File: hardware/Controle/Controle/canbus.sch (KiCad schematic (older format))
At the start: 5 parts, among them U201 MCP2561-E-SN

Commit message: first version of layout
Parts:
- added C202: 4.7n, Capacitor_SMD:C_0603_1608Metric_Pad1.08x0.95mm_HandSolder, symbol Device:C_Small
- added R203: 300, Resistor_SMD:R_0603_1608Metric_Pad0.98x0.95mm_HandSolder, symbol Device:R_Small
- added R204, R205: 60, Resistor_SMD:R_0603_1608Metric_Pad0.98x0.95mm_HandSolder, symbol Device:R_Small
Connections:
- net CAN_H: now also R204.2
- net CAN_L: now also R205.1
- net GND: now also C202.2
- net at U201.5 (SPLIT): now also R203.2
- new net: C202.1, R203.1, R204.1, R205.2
- no-connect marks 1 -> 0
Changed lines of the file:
@@
 $EndDescr
 Wire Wire Line
-	5750 3350 6450 3350
-Wire Wire Line
-	5750 3550 6450 3550
+	5750 3000 6200 3000
+Wire Wire Line
+	5750 3900 6200 3900
 Connection ~ 5250 4000
 $Comp
@@
 	0    -1   -1   0
 $EndComp
-Text Label 6200 3350 0    50   ~ 0
+Text Label 6500 3000 2    50   ~ 0
 CAN_H
-Text Label 6200 3550 0    50   ~ 0
+Text Label 6550 3900 2    50   ~ 0
 CAN_L
-Text HLabel 6450 3350 2    50   Input ~ 0
+Text HLabel 6500 3000 2    50   Input ~ 0
 CAN_H
-Text HLabel 6450 3550 2    50   Input ~ 0
+Text HLabel 6550 3900 2    50   Input ~ 0
 CAN_L
 Text HLabel 4200 3250 0    50   Input ~ 0
@@
 	1    0    0    -1
 $EndComp
-NoConn ~ 5750 3450
 Wire Wire Line
 	7050 4600 7050 4500
+Wire Wire Line
+	5750 3000 5750 3350
+Wire Wire Line
+	5750 3900 5750 3550
+$Comp
+L Device:R_Small R?
+U 1 1 60A1B053
+P 6000 3450
+AR Path="/60A1B053" Ref="R?"  Part="1"
+AR Path="/606C6891/60A1B053" Ref="R203"  Part="1"
+F 0 "R203" H 6059 3496 50  0000 L CNN
+F 1 "300" H 6059 3405 50  0000 L CNN
+F 2 "Resistor_SMD:R_0603_1608Metric_Pad0.98x0.95mm_HandSolder" H 6000 3450 50  0001 C CNN
+F 3 "~" H 6000 3450 50  0001 C CNN
+	1    6000 3450
+	0    1    1    0
+$EndComp
+Wire Wire Line
+	5900 3450 5750 3450
+$Comp
+L Device:R_Small R?
+U 1 1 60A1D2BE
+P 6200 3250
+AR Path="/60A1D2BE" Ref="R?"  Part="1"
+AR Path="/606C6891/60A1D2BE" Ref="R204"  Part="1"
+F 0 "R204" H 6259 3296 50  0000 L CNN
+F 1 "60" H 6259 3205 50  0000 L CNN
+F 2 "Resistor_SMD:R_0603_1608Metric_Pad0.98x0.95mm_HandSolder" H 6200 3250 50  0001 C CNN
+F 3 "~" H 6200 3250 50  0001 C CNN
+	1    6200 3250
+	1    0    0    1
+$EndComp
+Wire Wire Line
+	6200 3550 6200 3450
+Wire Wire Line
+	6100 3450 6200 3450
+Connection ~ 6200 3450
+Wire Wire Line
+	6200 3450 6200 3350
+Wire Wire Line
+	6200 3750 6200 3900
+Connection ~ 6200 3900
+Wire Wire Line
+	6200 3900 6550 3900
+$Comp
+L Device:R_Small R?
+U 1 1 60A1D7FB
+P 6200 3650
+AR Path="/60A1D7FB" Ref="R?"  Part="1"
+AR Path="/606C6891/60A1D7FB" Ref="R205"  Part="1"
+F 0 "R205" H 6259 3696 50  0000 L CNN
+F 1 "60" H 6259 3605 50  0000 L CNN
+F 2 "Resistor_SMD:R_0603_1608Metric_Pad0.98x0.95mm_HandSolder" H 6200 3650 50  0001 C CNN
+F 3 "~" H 6200 3650 50  0001 C CNN
+	1    6200 3650
+	1    0    0    1
+$EndComp
+Wire Wire Line
+	6200 3150 6200 3000
+Connection ~ 6200 3000
+Wire Wire Line
+	6200 3000 6500 3000
+$Comp
+L Device:C_Small C?
+U 1 1 60A214AF
+P 6600 3450
+AR Path="/60A214AF" Ref="C?"  Part="1"
+AR Path="/606C6891/60A214AF" Ref="C202"  Part="1"
+F 0 "C202" V 6829 3450 50  0000 C CNN
+F 1 "4.7n" V 6738 3450 50  0000 C CNN
+F 2 "Capacitor_SMD:C_0603_1608Metric_Pad1.08x0.95mm_HandSolder" H 6600 3450 50  0001 C CNN
+F 3 "~" H 6600 3450 50  0001 C CNN
+	1    6600 3450
+	0    -1   -1   0
+$EndComp
+Wire Wire Line
+	6500 3450 6200 3450
+$Comp
+L power:GND #PWR?
+U 1 1 60A223CF
+P 6900 3500
+AR Path="/60A223CF" Ref="#PWR?"  Part="1"
+AR Path="/606C6891/60A223CF" Ref="#PWR0129"  Part="1"
+F 0 "#PWR0129" H 6900 3250 50  0001 C CNN
+F 1 "GND" H 6905 3327 50  0000 C CNN
+F 2 "" H 6900 3500 50  0001 C CNN
+F 3 "" H 6900 3500 50  0001 C CNN
+	1    6900 3500
+	1    0    0    -1
+$EndComp
+Wire Wire Line
+	6900 3500 6900 3450
+Wire Wire Line
+	6900 3450 6700 3450
 $EndSCHEMATC

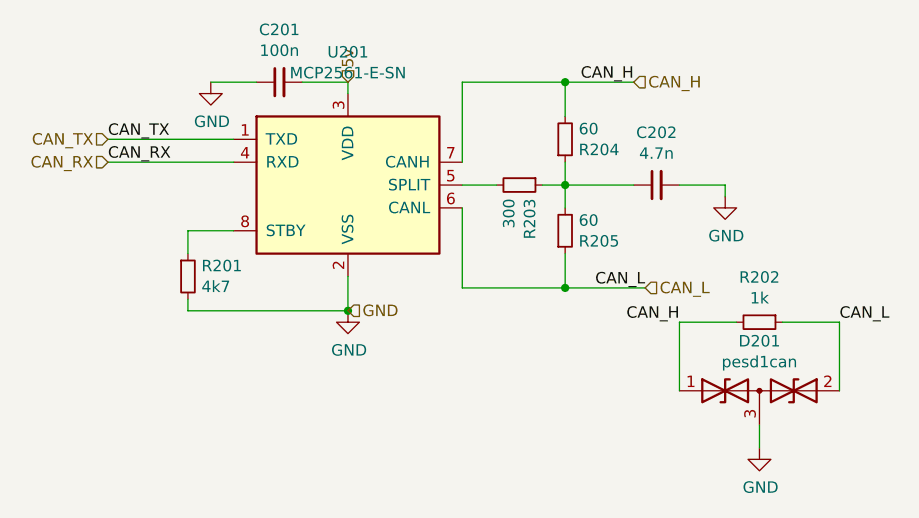
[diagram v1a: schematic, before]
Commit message: small changes (compnents values)
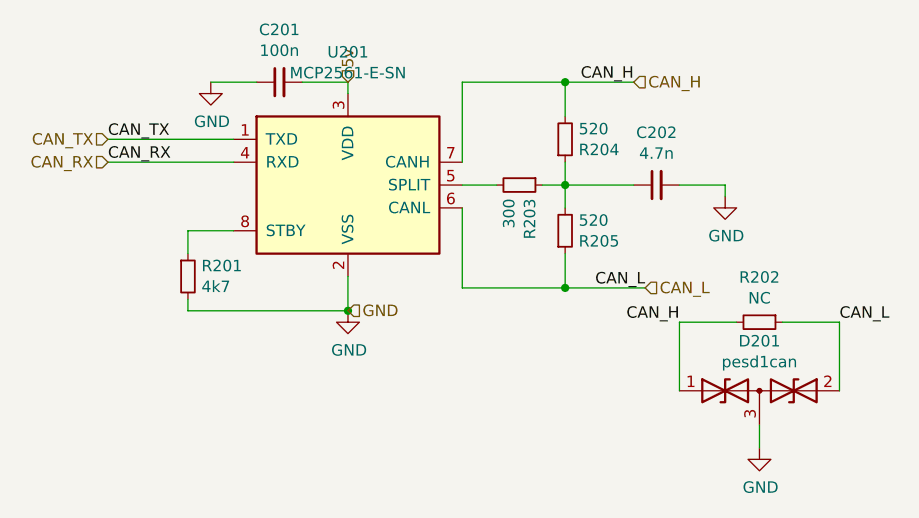
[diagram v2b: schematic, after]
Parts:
- R202: value 1k -> NC
- R204, R205: value 60 -> 520
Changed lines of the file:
@@
 P 7050 4050
 F 0 "R202" V 6854 4050 50  0000 C CNN
-F 1 "1k" V 6945 4050 50  0000 C CNN
+F 1 "NC" V 6945 4050 50  0000 C CNN
 F 2 "Resistor_SMD:R_0603_1608Metric_Pad0.98x0.95mm_HandSolder" H 7050 4050 50  0001 C CNN
 F 3 "~" H 7050 4050 50  0001 C CNN
@@
 AR Path="/606C6891/60A1D2BE" Ref="R204"  Part="1"
 F 0 "R204" H 6259 3296 50  0000 L CNN
-F 1 "60" H 6259 3205 50  0000 L CNN
+F 1 "520" H 6259 3205 50  0000 L CNN
 F 2 "Resistor_SMD:R_0603_1608Metric_Pad0.98x0.95mm_HandSolder" H 6200 3250 50  0001 C CNN
 F 3 "~" H 6200 3250 50  0001 C CNN
@@
 AR Path="/606C6891/60A1D7FB" Ref="R205"  Part="1"
 F 0 "R205" H 6259 3696 50  0000 L CNN
-F 1 "60" H 6259 3605 50  0000 L CNN
+F 1 "520" H 6259 3605 50  0000 L CNN
 F 2 "Resistor_SMD:R_0603_1608Metric_Pad0.98x0.95mm_HandSolder" H 6200 3650 50  0001 C CNN
 F 3 "~" H 6200 3650 50  0001 C CNN
